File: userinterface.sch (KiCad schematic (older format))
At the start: 40 parts

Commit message: Se hace cambios en el esquematico y se anexa PCB
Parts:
- removed M? (x8): MNMOS, symbol pspice:MNMOS
- added Q401, Q402, Q403, Q404, Q405, Q406, Q407, Q408: FDV301N, Package_TO_SOT_SMD:SOT-23, symbol Device:Q_NMOS_GDS
- D401, D402, D403, D404, D405, D406, D407, D408: renamed from D?; footprint (none) -> LED_SMD:LED_0805_2012Metric_Pad1.15x1.40mm_HandSolder
- R401, R402, R403, R404, R405, R406, R407, R408, R409, R410, R411, R412, R413, R414, R415, R416: renamed from R?; footprint (none) -> Resistor_SMD:R_0805_2012Metric_Pad1.15x1.40mm_HandSolder
- SW401, SW402, SW403, SW404, SW405, SW406, SW407, SW408: renamed from SW?; footprint (none) -> Button_Switch_SMD:SW_SPST_B3U-1000P
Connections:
- net labels added: LED[0..7], SW0, SW1, SW2, SW3, SW4, SW5, SW6, SW7, SW[0..7]
- wire segments 88 -> 80
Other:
- moved on the sheet: D402, D403, D404, D405, D406, D407, D408, R402, R403, R404, R405, R406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

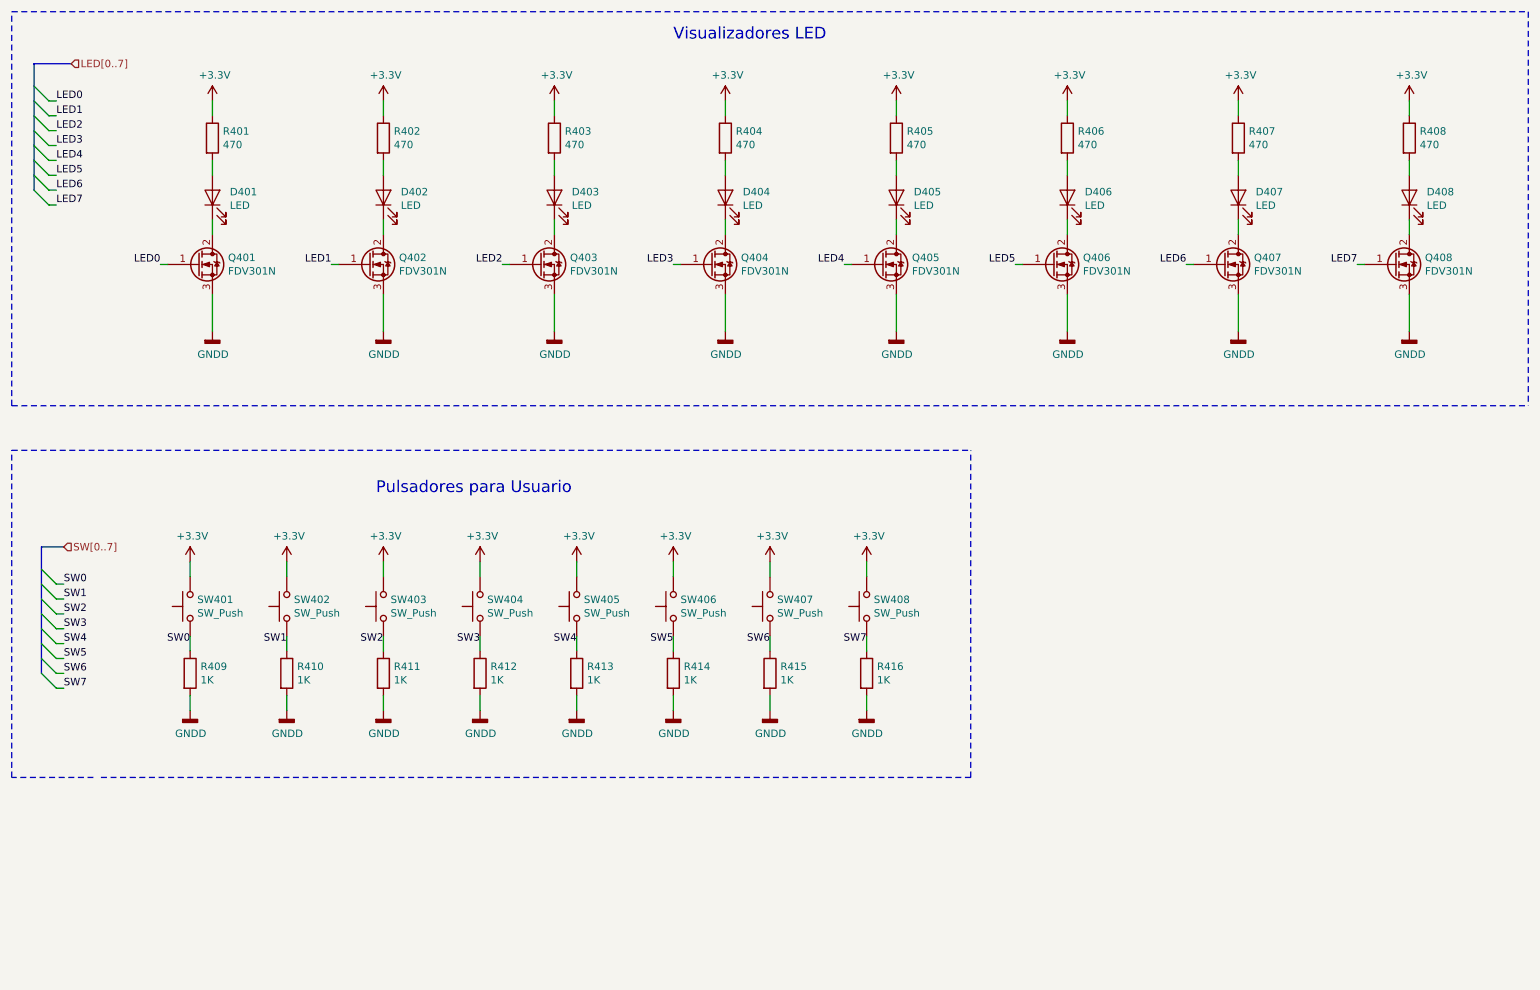
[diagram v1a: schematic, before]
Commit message: Se realizan correcciones finales y se agregan carpetas BOM, Datasheet, Doc, Gerbers, lib.pretty y shapes3D
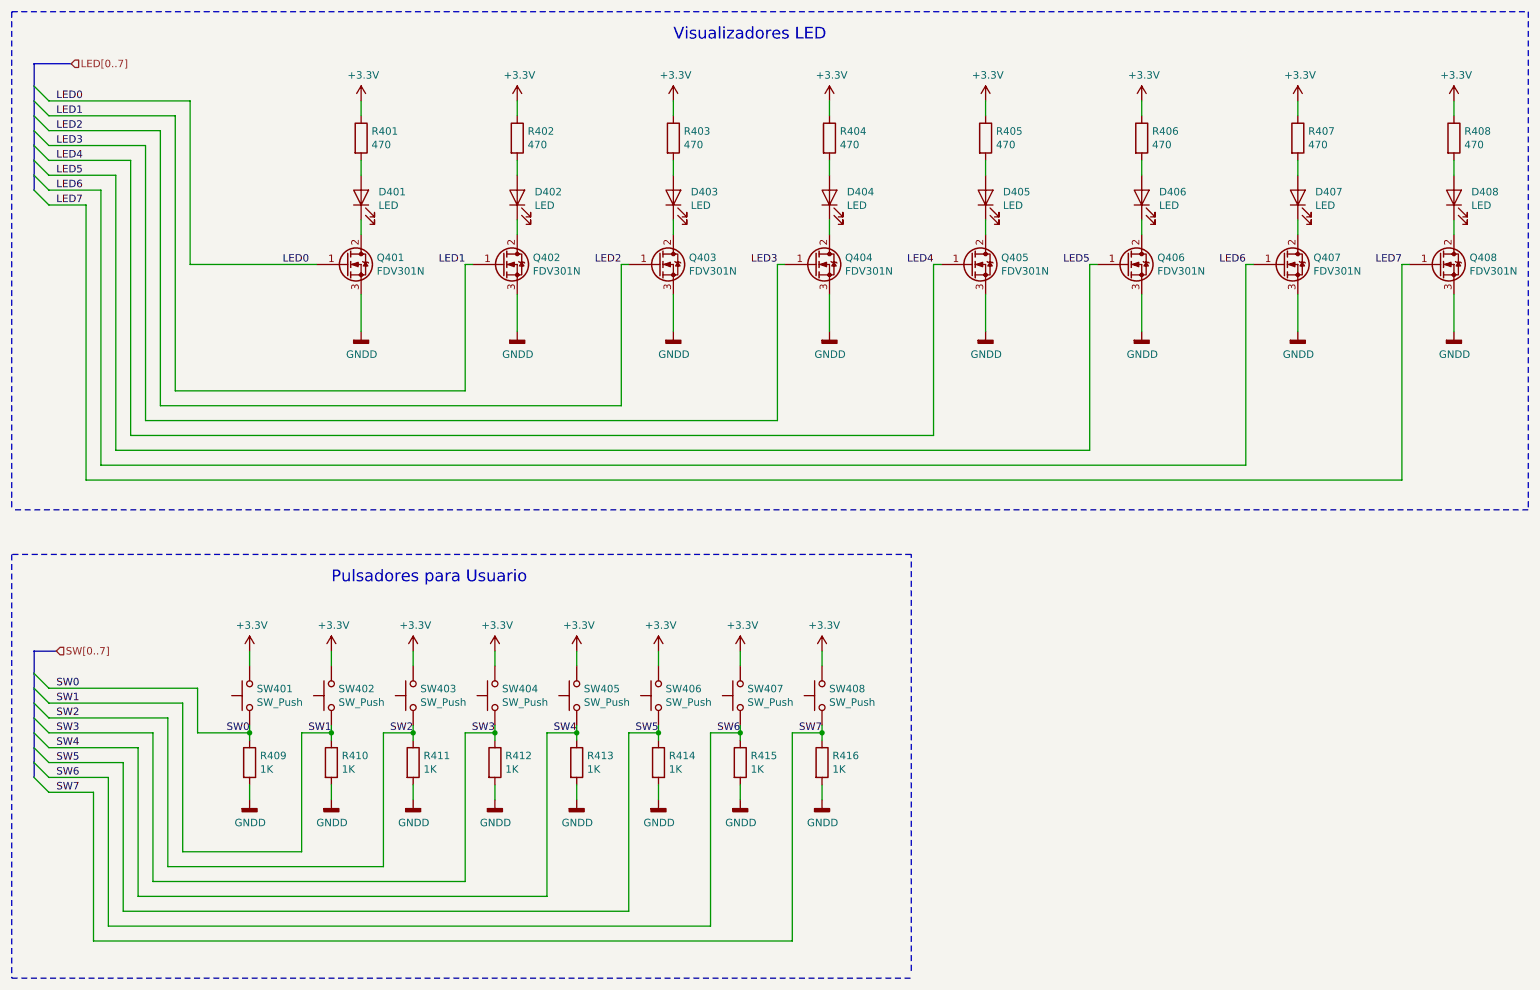
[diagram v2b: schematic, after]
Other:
- moved on the sheet: D401, D402, D403, D404, D405, D406, D407, D408, Q401, Q402, Q403, Q404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
